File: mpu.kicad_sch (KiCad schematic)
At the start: 5 parts, among them U10 MPU6050

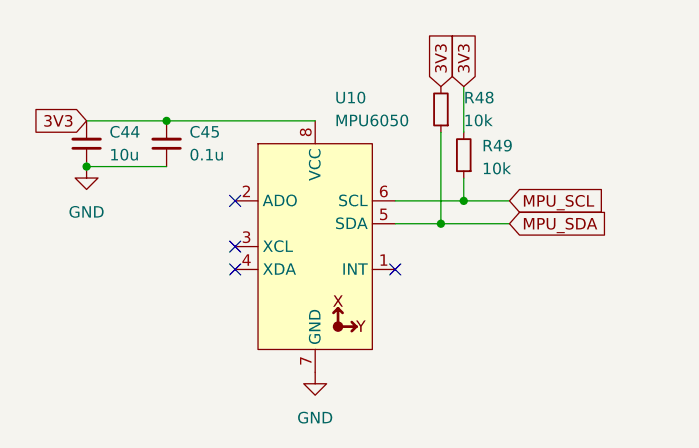
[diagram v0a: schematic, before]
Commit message: gpio expander added comm finished
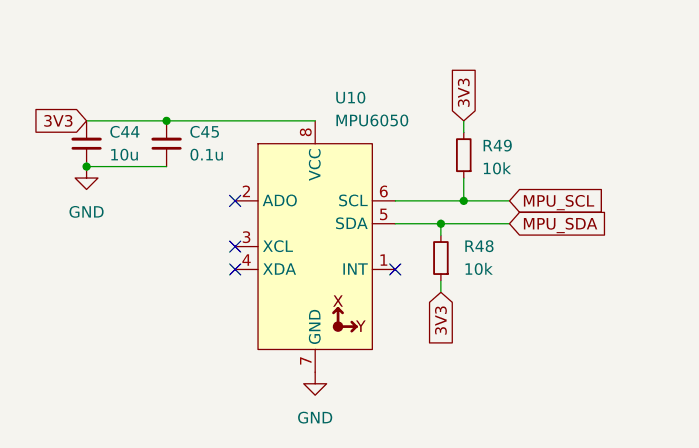
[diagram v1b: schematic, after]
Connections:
- net 3V3: now also R48.1; no longer R48.2
- net MPU_SDA: now also R48.2; no longer R48.1
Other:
- moved on the sheet: R48
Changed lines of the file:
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@@
+	(wire
+		(pts
+			(xy 59.69 36.83) (xy 59.69 35.56)
+		)
+		(stroke
+			(width 0)
+			(type default)
+		)
+	)
 	(wire
 		(pts
@@
 	(wire
 		(pts
+			(xy 59.69 41.91) (xy 59.69 43.18)
+		)
+		(stroke
+			(width 0)
+			(type default)
+		)
+	)
+	(wire
+		(pts
 			(xy 54.61 33.02) (xy 62.23 33.02)
 		)
@@
 	(wire
 		(pts
-			(xy 59.69 25.4) (xy 59.69 35.56)
-		)
-		(stroke
-			(width 0)
-			(type default)
-		)
-	)
-	(wire
-		(pts
 			(xy 62.23 33.02) (xy 67.31 33.02)
 		)
@@
 	(wire
 		(pts
-			(xy 62.23 20.32) (xy 62.23 25.4)
+			(xy 62.23 24.13) (xy 62.23 25.4)
 		)
 		(stroke
@@
 	(global_label "3V3"
 		(shape input)
-		(at 59.69 20.32 90)
+		(at 59.69 43.18 270)
 		(fields_autoplaced yes)
 		(effects
@@
 				(size 1.27 1.27)
 			)
-			(justify left)
+			(justify right)
 		)
 		(property "Intersheetrefs" "${INTERSHEET_REFS}"
-			(at 59.69 13.8272 90)
-			(effects
-				(font
-					(size 1.27 1.27)
-				)
-				(justify left)
+			(at 59.69 49.6728 90)
+			(effects
+				(font
+					(size 1.27 1.27)
+				)
+				(justify right)
 				(hide yes)
 			)
@@
 	(global_label "3V3"
 		(shape input)
-		(at 62.23 20.32 90)
+		(at 62.23 24.13 90)
 		(fields_autoplaced yes)
 		(effects
@@
 		)
 		(property "Intersheetrefs" "${INTERSHEET_REFS}"
-			(at 62.23 13.8272 90)
+			(at 62.23 17.6372 90)
 			(effects
 				(font
@@
 	(symbol
 		(lib_id "Device:R_Small")
-		(at 59.69 22.86 180)
+		(at 59.69 39.37 180)
 		(unit 1)
 		(exclude_from_sim no)
@@
 		(fields_autoplaced yes)
 		(property "Reference" "R48"
-			(at 62.23 21.5899 0)
+			(at 62.23 38.0999 0)
 			(effects
 				(font
@@
 		)
 		(property "Value" "10k"
-			(at 62.23 24.1299 0)
+			(at 62.23 40.6399 0)
 			(effects
 				(font
@@
 		)
 		(property "Footprint" "Resistor_SMD:R_0805_2012Metric"
-			(at 59.69 22.86 0)
+			(at 59.69 39.37 0)
 			(effects
 				(font
@@
 		)
 		(property "Datasheet" "~"
-			(at 59.69 22.86 0)
+			(at 59.69 39.37 0)
 			(effects
 				(font
@@
 		)
 		(property "Description" "Resistor, small symbol"
-			(at 59.69 22.86 0)
-			(effects
-				(font
+			(at 59.69 39.37 0)
+			(effects
+				(font

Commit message: Visual Improvements
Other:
- note added: "MPU6050 Module"
- moved on the sheet: C44, C45, R48, R49, U10

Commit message: schematic finished
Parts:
- renumbered R49 to R66, R48 to R67
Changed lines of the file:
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@@
 		(on_board yes)
 		(dnp no)
-		(property "Reference" "R49"
+		(property "Reference" "R66"
 			(at 66.802 26.924 0)
 			(effects
@@
 			(project "controllerForVehicle"
 				(path "/f177fb06-71dc-4865-9331-a828b12c2bf7/5b9378f8-f7b1-4754-9b49-5b2cb88e490a"
-					(reference "R49")
+					(reference "R66")
 					(unit 1)
 				)
@@
 		(dnp no)
 		(fields_autoplaced yes)
-		(property "Reference" "#PWR045"
+		(property "Reference" "#PWR048"
 			(at 48.26 58.42 0)
 			(effects
@@
 			(project "controllerForVehicle"
 				(path "/f177fb06-71dc-4865-9331-a828b12c2bf7/5b9378f8-f7b1-4754-9b49-5b2cb88e490a"
-					(reference "#PWR045")
+					(reference "#PWR048")
 					(unit 1)
 				)
@@
 		(dnp no)
 		(fields_autoplaced yes)
-		(property "Reference" "#PWR044"
+		(property "Reference" "#PWR047"
 			(at 22.86 35.56 0)
 			(effects
@@
 			(project "controllerForVehicle"
 				(path "/f177fb06-71dc-4865-9331-a828b12c2bf7/5b9378f8-f7b1-4754-9b49-5b2cb88e490a"
-					(reference "#PWR044")
+					(reference "#PWR047")
 					(unit 1)
 				)
@@
 		(dnp no)
 		(fields_autoplaced yes)
-		(property "Reference" "R48"
+		(property "Reference" "R67"
 			(at 64.77 38.0999 0)
 			(effects
@@
 			(project "controllerForVehicle"
 				(path "/f177fb06-71dc-4865-9331-a828b12c2bf7/5b9378f8-f7b1-4754-9b49-5b2cb88e490a"
-					(reference "R48")
-					(unit 1)
-				)
+					(reference "R67")
+					(unit 1)
+				)

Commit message: silinecek
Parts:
- renumbered R66 to R63, R67 to R64
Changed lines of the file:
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@@
 		(on_board yes)
 		(dnp no)
-		(property "Reference" "R66"
+		(property "Reference" "R63"
 			(at 66.802 26.924 0)
 			(effects
@@
 			(project "controllerForVehicle"
 				(path "/f177fb06-71dc-4865-9331-a828b12c2bf7/5b9378f8-f7b1-4754-9b49-5b2cb88e490a"
-					(reference "R66")
+					(reference "R63")
 					(unit 1)
 				)
@@
 		(dnp no)
 		(fields_autoplaced yes)
-		(property "Reference" "#PWR048"
+		(property "Reference" "#PWR054"
 			(at 48.26 58.42 0)
 			(effects
@@
 			(project "controllerForVehicle"
 				(path "/f177fb06-71dc-4865-9331-a828b12c2bf7/5b9378f8-f7b1-4754-9b49-5b2cb88e490a"
-					(reference "#PWR048")
+					(reference "#PWR054")
 					(unit 1)
 				)
@@
 		(dnp no)
 		(fields_autoplaced yes)
-		(property "Reference" "#PWR047"
+		(property "Reference" "#PWR053"
 			(at 22.86 35.56 0)
 			(effects
@@
 			(project "controllerForVehicle"
 				(path "/f177fb06-71dc-4865-9331-a828b12c2bf7/5b9378f8-f7b1-4754-9b49-5b2cb88e490a"
-					(reference "#PWR047")
+					(reference "#PWR053")
 					(unit 1)
 				)
@@
 		(dnp no)
 		(fields_autoplaced yes)
-		(property "Reference" "R67"
+		(property "Reference" "R64"
 			(at 64.77 38.0999 0)
 			(effects
@@
 			(project "controllerForVehicle"
 				(path "/f177fb06-71dc-4865-9331-a828b12c2bf7/5b9378f8-f7b1-4754-9b49-5b2cb88e490a"
-					(reference "R67")
-					(unit 1)
-				)
+					(reference "R64")
+					(unit 1)
+				)
